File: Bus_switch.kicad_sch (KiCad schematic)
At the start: 7 parts, among them J3 Conn_01x04_Pin, U1 SN74CB3Q3384APW

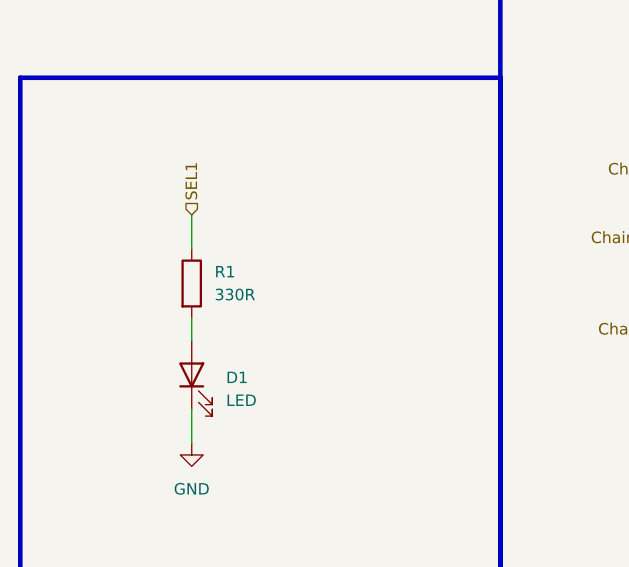
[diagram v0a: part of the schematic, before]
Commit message: Added mechanical standard and updated readme
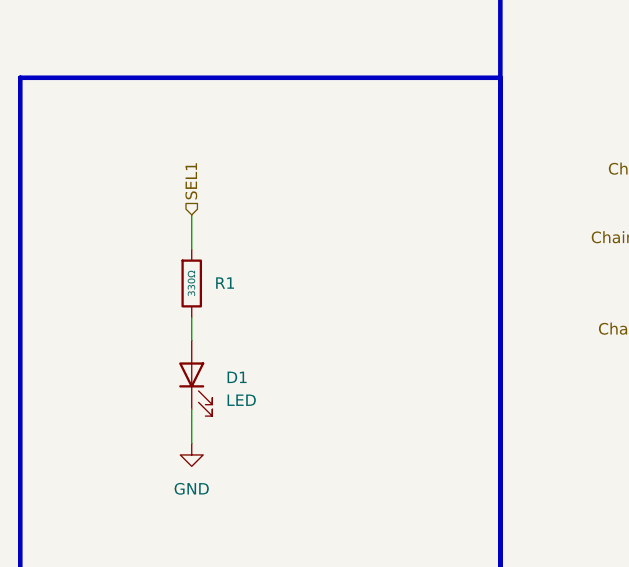
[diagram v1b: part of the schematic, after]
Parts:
- removed R1: 330R, symbol Device:R
- added R1: 330Ω, PCM_JLCPCB:R_0402, symbol PCM_JLCPCB-Resistors:0402,330Ω
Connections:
- net SEL1: now also R1.1
- net at D1.2 (A): now also R1.2
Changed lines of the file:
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@@
+			)
+		)
+		(property "Sim.Device" ""
+			(at 227.33 124.46 0)
+			(effects
+				(font
+					(size 1.27 1.27)
+				)
+				(hide yes)
 			)
 		)
@@
 			)
 		)
+		(property "Sim.Device" ""
+			(at 34.29 97.79 90)
+			(effects
+				(font
+					(size 1.27 1.27)
+				)
+				(hide yes)
+			)
+		)
 		(pin "2"
 		)
@@
 			)
 		)
+		(property "Sim.Device" ""
+			(at 257.81 63.5 0)
+			(effects
+				(font
+					(size 1.27 1.27)
+				)
+				(hide yes)
+			)
+		)
 		(pin "1"
 		)
@@
 	)
 	(symbol
+		(lib_id "PCM_JLCPCB-Resistors:0402,330Ω")
+		(at 34.29 87.63 0)
+		(unit 1)
+		(exclude_from_sim no)
+		(in_bom yes)
+		(on_board yes)
+		(dnp no)
+		(fields_autoplaced yes)
+		(property "Reference" "R1"
+			(at 36.83 87.6299 0)
+			(effects
+				(font
+					(size 1.27 1.27)
+				)
+				(justify left)
+			)
+		)
+		(property "Value" "330Ω"
+			(at 34.29 87.63 90)
+			(do_not_autoplace yes)
+			(effects
+				(font
+					(size 0.8 0.8)
+				)
+			)
+		)
+		(property "Footprint" "PCM_JLCPCB:R_0402"
+			(at 32.512 87.63 90)
+			(effects
+				(font
+					(size 1.27 1.27)
+				)
+				(hide yes)
+			)
+		)
+		(property "Datasheet" "https://www.lcsc.com/datasheet/lcsc_datasheet_2205311900_UNI-ROYAL-Uniroyal-Elec-0402WGF3300TCE_C25104.pdf"
+			(at 34.29 87.63 0)
+			(effects
+				(font
+					(size 1.27 1.27)
+				)
+				(hide yes)
+			)
+		)
+		(property "Description" "62.5mW Thick Film Resistors 50V ±100ppm/°C ±1% 330Ω 0402 Chip Resistor - Surface Mount ROHS"
+			(at 34.29 87.63 0)
+			(effects
+				(font
+					(size 1.27 1.27)
+				)
+				(hide yes)
+			)
+		)
+		(property "LCSC" "C25104"
+			(at 34.29 87.63 0)
+			(effects
+				(font
+					(size 1.27 1.27)
+				)
+				(hide yes)
+			)
+		)
+		(property "Stock" "1159127"
+			(at 34.29 87.63 0)
+			(effects
+				(font
+					(size 1.27 1.27)
+				)
+				(hide yes)
+			)
+		)
+		(property "Price" "0.004USD"
+			(at 34.29 87.63 0)
+			(effects
+				(font
+					(size 1.27 1.27)
+				)
+				(hide yes)
+			)
+		)
+		(property "Process" "SMT"
+			(at 34.29 87.63 0)
+			(effects
+				(font
+					(size 1.27 1.27)
+				)
+				(hide yes)
+			)
+		)
+		(property "Minimum Qty" "20"
+			(at 34.29 87.63 0)
+			(effects
+				(font
+					(size 1.27 1.27)
+				)
+				(hide yes)
+			)
+		)
+		(property "Attrition Qty" "10"
+			(at 34.29 87.63 0)
+			(effects
+				(font
+					(size 1.27 1.27)
+				)
+				(hide yes)
+			)
+		)
+		(property "Class" "Basic Component"
+			(at 34.29 87.63 0)
+			(effects
+				(font
+					(size 1.27 1.27)
+				)
+				(hide yes)
+			)
+		)
+		(property "Category" "Resistors,Chip Resistor - Surface Mount"
+			(at 34.29 87.63 0)
+			(effects
+				(font
+					(size 1.27 1.27)
+				)
+				(hide yes)
+			)
+		)
+		(property "Manufacturer" "UNI-ROYAL(Uniroyal Elec)"
+			(at 34.29 87.63 0)
+			(effects
+				(font
+					(size 1.27 1.27)
+				)
+				(hide yes)
+			)
+		)
+		(property "Part" "0402WGF3300TCE"
+			(at 34.29 87.63 0)
+			(effects
+				(font
+					(size 1.27 1.27)
+				)
+				(hide yes)
+			)
+		)
+		(property "Resistance" "330Ω"
+			(at 34.29 87.63 0)
+			(effects
+				(font
+					(size 1.27 1.27)
+				)
+				(hide yes)
+			)
+		)
+		(property "Power(Watts)" "62.5mW"
+			(at 34.29 87.63 0)
+			(effects
+				(font
+					(size 1.27 1.27)
+				)
+				(hide yes)
+			)
+		)
+		(property "Type" "Thick Film Resistors"
+			(at 34.29 87.63 0)
+			(effects
+				(font
+					(size 1.27 1.27)
+				)
+				(hide yes)
+			)
+		)
+		(property "Overload Voltage (Max)" "50V"
+			(at 34.29 87.63 0)
+			(effects
+				(font
+					(size 1.27 1.27)
+				)
+				(hide yes)
+			)
+		)
+		(property "Operating Temperature Range" "-55°C~+155°C"
+			(at 34.29 87.63 0)
+			(effects
+				(font
+					(size 1.27 1.27)
+				)
+				(hide yes)
+			)
+		)
+		(property "Tolerance" "±1%"
+			(at 34.29 87.63 0)
+			(effects
+				(font
+					(size 1.27 1.27)
+				)
+				(hide yes)
+			)
+		)
+		(property "Temperature Coefficient" "±100ppm/°C"
+			(at 34.29 87.63 0)
+			(effects
+				(font
+					(size 1.27 1.27)
+				)
+				(hide yes)
+			)
+		)
+		(property "Sim.Device" ""
+			(at 34.29 87.63 0)
+			(effects
+				(font
+					(size 1.27 1.27)
+				)
+				(hide yes)
+			)
+		)
+		(pin "1"
+		)
+		(pin "2"
+		)
+		(instances
+			(project ""
+				(path "/6596548a-44e0-46d8-8624-fd71cf4a3e17/ec6d73af-72b0-4068-85fb-cca3c5143749"
+					(reference "R1")
+					(unit 1)
+				)
+			)
+		)
+	)
+	(symbol
 		(lib_id "PCM_JLCPCB-Resistors:0402,10kΩ")
 		(at 215.9 124.46 0)
@@
 		)
 		(property "Temperature Coefficient" "±100ppm/°C"
+			(at 215.9 124.46 0)
+			(effects
+				(font
+					(size 1.27 1.27)
+				)
+				(hide yes)
+			)
+		)
+		(property "Sim.Device" ""
 			(at 215.9 124.46 0)
 			(effects
@@
 	)
 	(symbol
-		(lib_id "Device:R")
-		(at 34.29 87.63 0)
-		(unit 1)
-		(exclude_from_sim no)
-		(in_bom yes)
-		(on_board yes)
-		(dnp no)
-		(fields_autoplaced yes)
-		(property "Reference" "R1"
-			(at 36.83 86.3599 0)
-			(effects
-				(font
-					(size 1.27 1.27)
-				)
-				(justify left)
-			)
-		)
-		(property "Value" "330R"
-			(at 36.83 88.8999 0)
-			(effects
-				(font
-					(size 1.27 1.27)
-				)
-				(justify left)
-			)
-		)
-		(property "Footprint" ""
-			(at 32.512 87.63 90)
-			(effects
-				(font
-					(size 1.27 1.27)
-				)
-				(hide yes)
-			)
-		)
-		(property "Datasheet" "~"
-			(at 34.29 87.63 0)
-			(effects
-				(font
-					(size 1.27 1.27)
-				)
-				(hide yes)
-			)
-		)
-		(property "Description" "Resistor"
-			(at 34.29 87.63 0)
-			(effects
-				(font
-					(size 1.27 1.27)
-				)
-				(hide yes)
-			)
-		)
-		(pin "1"
-		)
-		(pin "2"
-		)
-		(instances
-			(project ""
-				(path "/6596548a-44e0-46d8-8624-fd71cf4a3e17/ec6d73af-72b0-4068-85fb-cca3c5143749"
-					(reference "R1")
-					(unit 1)
-				)
-			)
-		)
-	)
-	(symbol
 		(lib_id "74xx:SN74CB3Q3384APW")
 		(at 132.08 97.79 0)
@@
 		)
 		(property "LCSC" "C469874"
+			(at 132.08 97.79 0)
+			(effects
+				(font
+					(size 1.27 1.27)
+				)
+				(hide yes)
+			)
+		)
+		(property "Sim.Device" ""
 			(at 132.08 97.79 0)
 			(effects
@@
 			(at 191.77 83.82 0)
 			(effects
+				(font
+					(size 1.27 1.27)
+				)
+				(hide yes)
+			)
+		)
+		(property "Sim.Device" ""
+			(at 191.77 83.82 0)
+			(effects

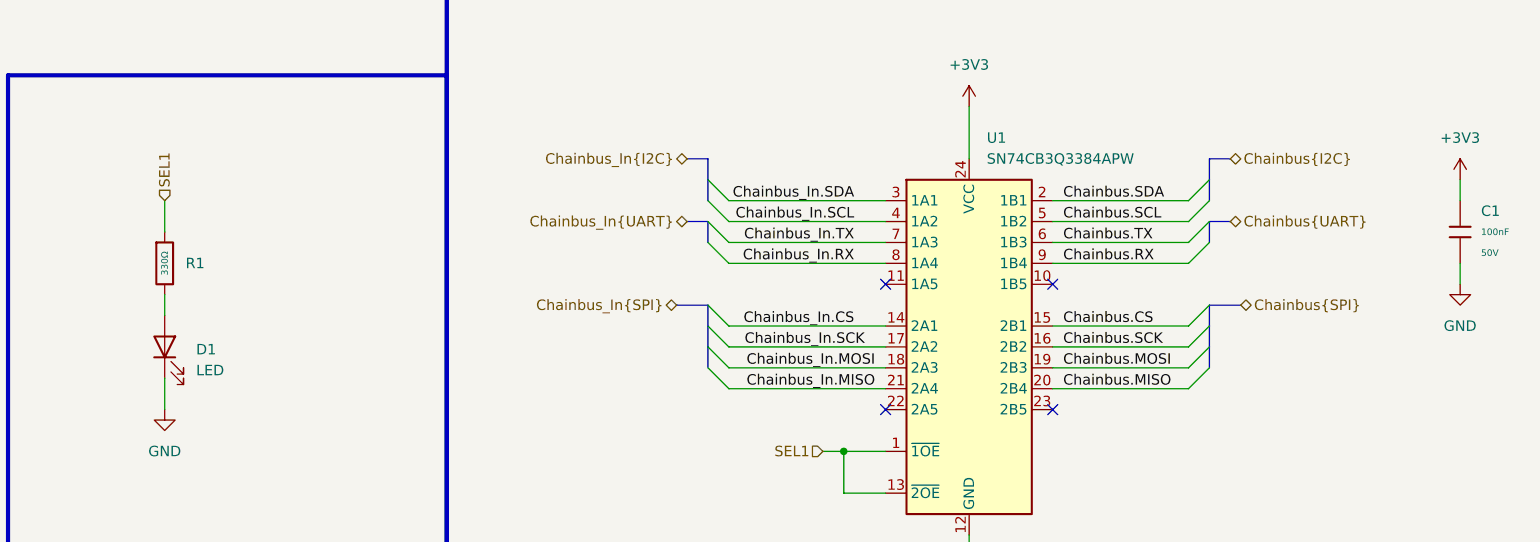
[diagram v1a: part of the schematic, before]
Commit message: updated XT60 place. added routing
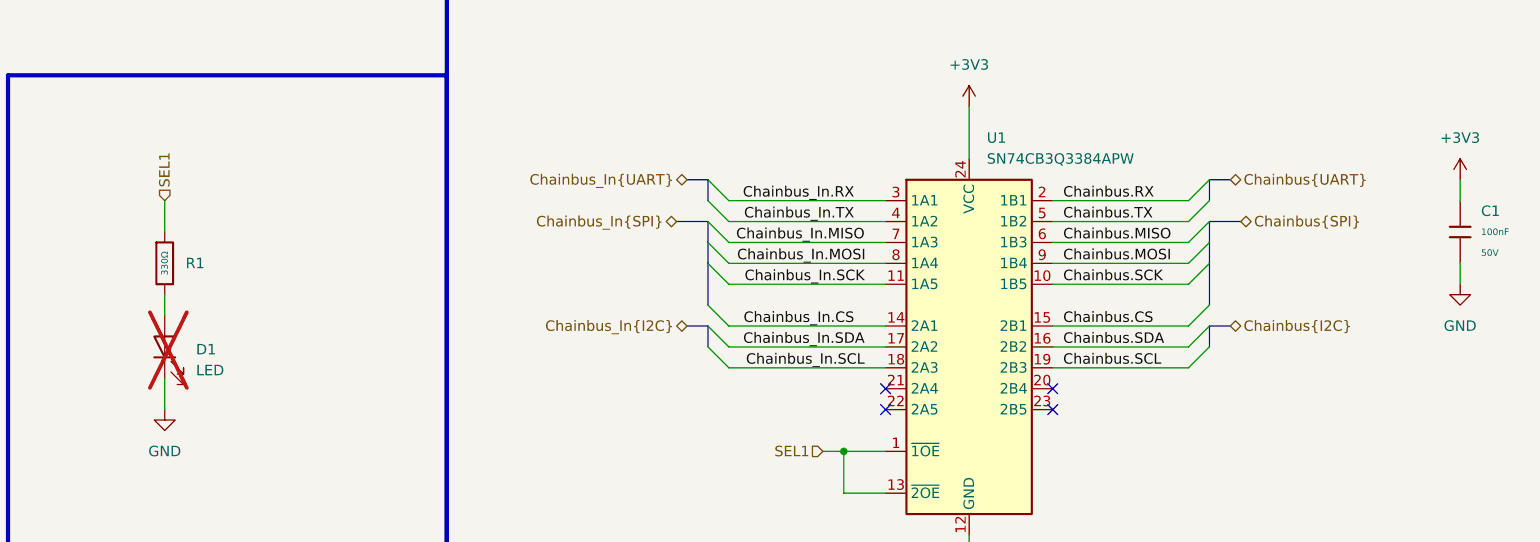
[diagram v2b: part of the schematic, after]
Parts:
- D1: now not fitted
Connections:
- net Chainbus.MISO: now also U1.6 (1B3); no longer U1.20 (2B4)
- net Chainbus.MOSI: now also U1.9 (1B4); no longer U1.19 (2B3)
- net Chainbus.RX: now also U1.2 (1B1); no longer U1.9 (1B4)
- net Chainbus.SCK: now also U1.10 (1B5); no longer U1.16 (2B2)
- net Chainbus.SCL: now also U1.19 (2B3); no longer U1.5 (1B2)
- net Chainbus.SDA: now also U1.16 (2B2); no longer U1.2 (1B1)
- net Chainbus.TX: now also U1.5 (1B2); no longer U1.6 (1B3)
- net Chainbus_In.MISO: now also U1.7 (1A3); no longer U1.21 (2A4)
- net Chainbus_In.MOSI: now also U1.8 (1A4); no longer U1.18 (2A3)
- net Chainbus_In.RX: now also U1.3 (1A1); no longer U1.8 (1A4)
- net Chainbus_In.SCK: now also U1.11 (1A5); no longer U1.17 (2A2)
- net Chainbus_In.SCL: now also U1.18 (2A3); no longer U1.4 (1A2)
- net Chainbus_In.SDA: now also U1.17 (2A2); no longer U1.3 (1A1)
- net Chainbus_In.TX: now also U1.4 (1A2); no longer U1.7 (1A3)
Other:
- title: (none) -> MMS3 Stepper Controler
